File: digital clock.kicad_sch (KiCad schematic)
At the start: 149 parts, among them Q1 BC557, Q10 BC547, Q11 BC547, Q12 BC557, Q13 BC557, Q14 BC557, Q2 BC557, Q3 BC557, Q7 BC557, Q8 BC547, Q9 BC547

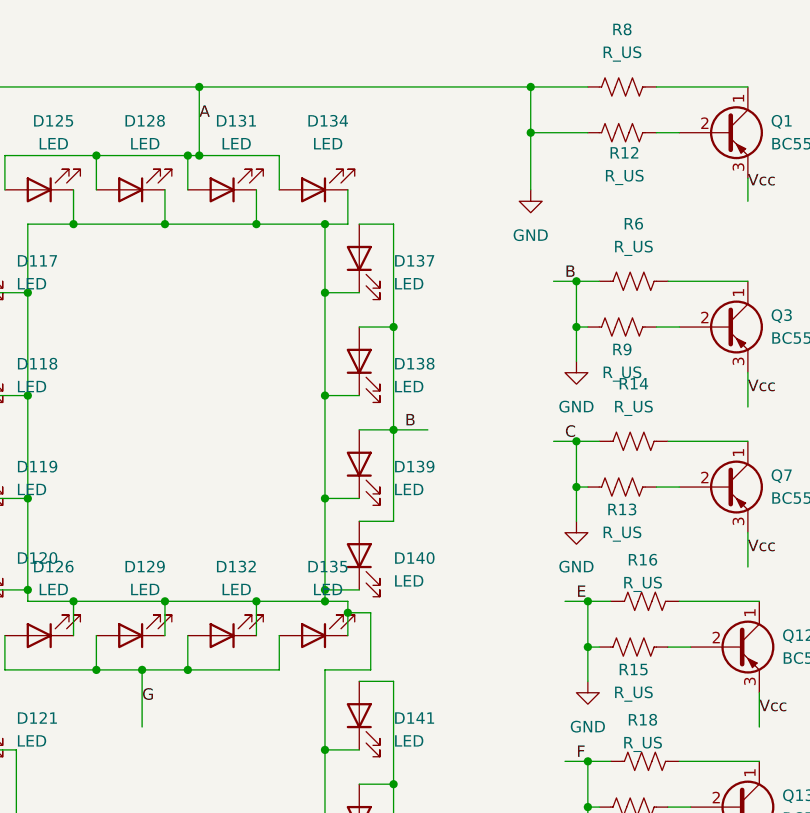
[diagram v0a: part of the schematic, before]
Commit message: correcting transistors
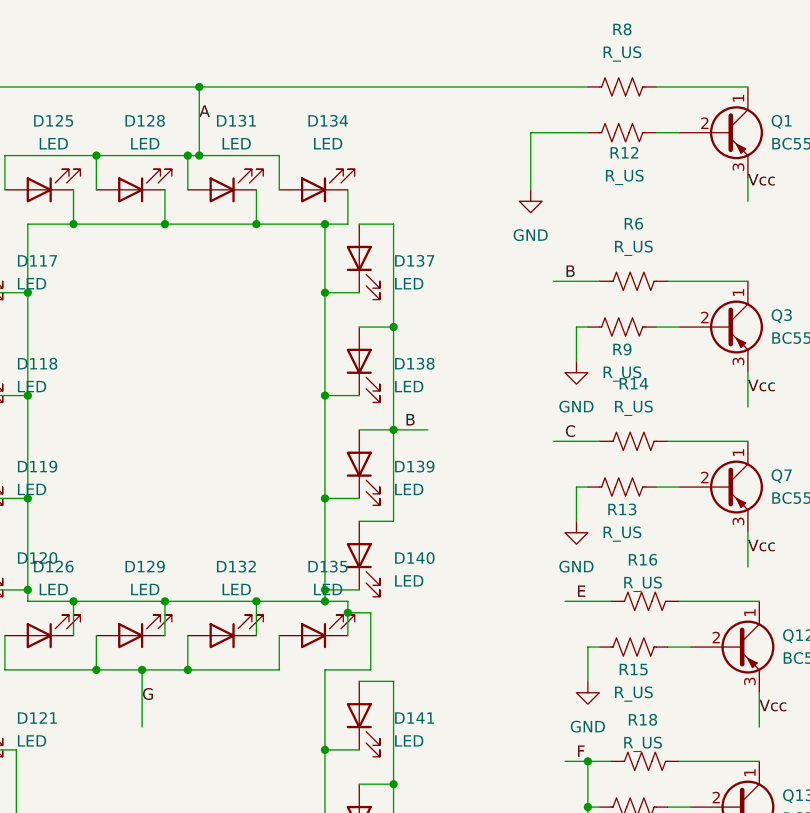
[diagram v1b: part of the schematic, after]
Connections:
- net GND: no longer D102.2 (A), D105.2 (A), D106.2 (A), D107.2 (A), D108.2 (A), D109.2 (A), D110.2 (A), D111.2 (A), D112.2 (A), D121.2 (A), D122.2 (A), D123.2 (A), D124.2 (A), D125.2 (A), D128.2 (A), D131.2 (A), D134.2 (A), D137.2 (A), D138.2 (A), D139.2 (A), D140.2 (A), D141.2 (A), D142.2 (A), D143.2 (A), D144.2 (A), D37.2 (A), D38.2 (A), D39.2 (A), D40.2 (A), D41.2 (A), D44.2 (A), D47.2 (A), D50.2 (A), D53.2 (A), D54.2 (A), D55.2 (A), D56.2 (A), D57.2 (A), D58.2 (A), D59.2 (A), D60.2 (A), D61.2 (A), D62.2 (A), D63.2 (A), D64.2 (A), D65.2 (A), D68.2 (A), D71.2 (A), D74.2 (A), D77.2 (A), D78.2 (A), D79.2 (A), D80.2 (A), D81.2 (A), D82.2 (A), D83.2 (A), D84.2 (A), D89.2 (A), D90.2 (A), D91.2 (A), D92.2 (A), D93.2 (A), D96.2 (A), D99.2 (A), R14.1, R16.1, R6.1, R8.1
- new net A: D102.2 (A), D125.2 (A), D128.2 (A), D131.2 (A), D134.2 (A), D41.2 (A), D44.2 (A), D47.2 (A), D50.2 (A), D65.2 (A), D68.2 (A), D71.2 (A), D74.2 (A), D93.2 (A), D96.2 (A), D99.2 (A), R8.1
- new net B: D105.2 (A), D106.2 (A), D107.2 (A), D108.2 (A), D137.2 (A), D138.2 (A), D139.2 (A), D140.2 (A), D54.2 (A), D56.2 (A), D58.2 (A), D60.2 (A), D77.2 (A), D78.2 (A), D79.2 (A), D80.2 (A), R6.1
- new net C: D109.2 (A), D110.2 (A), D111.2 (A), D112.2 (A), D141.2 (A), D142.2 (A), D143.2 (A), D144.2 (A), D61.2 (A), D62.2 (A), D63.2 (A), D64.2 (A), D81.2 (A), D82.2 (A), D83.2 (A), D84.2 (A), R14.1
- new net E: D121.2 (A), D122.2 (A), D123.2 (A), D124.2 (A), D37.2 (A), D38.2 (A), D39.2 (A), D40.2 (A), D53.2 (A), D55.2 (A), D57.2 (A), D59.2 (A), D89.2 (A), D90.2 (A), D91.2 (A), D92.2 (A), R16.1
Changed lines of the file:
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@@
 	(paper "A2")
 	(junction
-		(at 436.88 81.28)
-		(diameter 0)
-		(color 0 0 0 0)
-	)
-	(junction
 		(at 115.57 107.95)
 		(diameter 0)
@@
 	)
 	(junction
-		(at 443.23 138.43)
-		(diameter 0)
-		(color 0 0 0 0)
-	)
-	(junction
 		(at 157.48 137.16)
 		(diameter 0)
@@
 	)
 	(junction
-		(at 436.88 86.36)
-		(diameter 0)
-		(color 0 0 0 0)
-	)
-	(junction
 		(at 414.02 115.57)
 		(diameter 0)
@@
 	)
 	(junction
-		(at 441.96 102.87)
-		(diameter 0)
-		(color 0 0 0 0)
-	)
-	(junction
 		(at 323.85 88.9)
 		(diameter 0)
@@
 	)
 	(junction
-		(at 443.23 143.51)
-		(diameter 0)
-		(color 0 0 0 0)
-	)
-	(junction
 		(at 219.71 199.39)
 		(diameter 0)
@@
 	)
 	(junction
-		(at 441.96 120.65)
-		(diameter 0)
-		(color 0 0 0 0)
-	)
-	(junction
 		(at 115.57 119.38)
 		(diameter 0)
@@
 	)
 	(junction
-		(at 441.96 107.95)
-		(diameter 0)
-		(color 0 0 0 0)
-	)
-	(junction
 		(at 396.24 189.23)
 		(diameter 0)
@@
 	)
 	(junction
-		(at 441.96 125.73)
-		(diameter 0)
-		(color 0 0 0 0)
-	)
-	(junction
 		(at 237.49 96.52)
 		(diameter 0)
@@
 	(wire
 		(pts
-			(xy 441.96 120.65) (xy 441.96 125.73)
-		)
-		(stroke
-			(width 0)
-			(type default)
-		)
-	)
-	(wire
-		(pts
 			(xy 312.42 189.23) (xy 322.58 189.23)
 		)
@@
 	(wire
 		(pts
-			(xy 436.88 81.28) (xy 443.23 81.28)
-		)
-		(stroke
-			(width 0)
-			(type default)
-		)
-	)
-	(wire
-		(pts
 			(xy 162.56 139.7) (xy 160.02 139.7)
 		)
@@
 	(wire
 		(pts
-			(xy 440.69 138.43) (xy 443.23 138.43)
+			(xy 440.69 138.43) (xy 445.77 138.43)
 		)
 		(stroke
@@
 	(wire
 		(pts
-			(xy 400.05 81.28) (xy 436.88 81.28)
+			(xy 400.05 81.28) (xy 443.23 81.28)
 		)
 		(stroke
@@
 	(wire
 		(pts
-			(xy 441.96 102.87) (xy 441.96 107.95)
-		)
-		(stroke
-			(width 0)
-			(type default)
-		)
-	)
-	(wire
-		(pts
 			(xy 237.49 166.37) (xy 241.3 166.37)
 		)
@@
 	(wire
 		(pts
-			(xy 444.5 120.65) (xy 441.96 120.65)
-		)
-		(stroke
-			(width 0)
-			(type default)
-		)
-	)
-	(wire
-		(pts
 			(xy 199.39 127) (xy 204.47 127)
 		)
@@
 	(wire
 		(pts
-			(xy 444.5 102.87) (xy 441.96 102.87)
-		)
-		(stroke
-			(width 0)
-			(type default)
-		)
-	)
-	(wire
-		(pts
 			(xy 443.23 179.07) (xy 444.5 179.07)
 		)
@@
 	(wire
 		(pts
-			(xy 436.88 81.28) (xy 436.88 86.36)
-		)
-		(stroke
-			(width 0)
-			(type default)
-		)
-	)
-	(wire
-		(pts
 			(xy 312.42 189.23) (xy 312.42 191.77)
 		)
@@
 	(wire
 		(pts
-			(xy 443.23 138.43) (xy 443.23 143.51)
-		)
-		(stroke
-			(width 0)
-			(type default)
-		)
-	)
-	(wire
-		(pts
 			(xy 322.58 189.23) (xy 322.58 191.77)
 		)
@@
 	(wire
 		(pts
-			(xy 439.42 102.87) (xy 441.96 102.87)
+			(xy 439.42 102.87) (xy 444.5 102.87)
 		)
 		(stroke
@@
 	(wire
 		(pts
-			(xy 445.77 138.43) (xy 443.23 138.43)
-		)
-		(stroke
-			(width 0)
-			(type default)
-		)
-	)
-	(wire
-		(pts
 			(xy 157.48 177.8) (xy 157.48 187.96)
 		)
@@
 	(wire
 		(pts
-			(xy 439.42 120.65) (xy 441.96 120.65)
+			(xy 439.42 120.65) (xy 444.5 120.65)
 		)
 		(stroke
@@
 		(on_board yes)
 		(dnp no)
-		(fields_autoplaced yes)
 		(property "Reference" "Q1"
 			(at 463.55 85.0899 0)

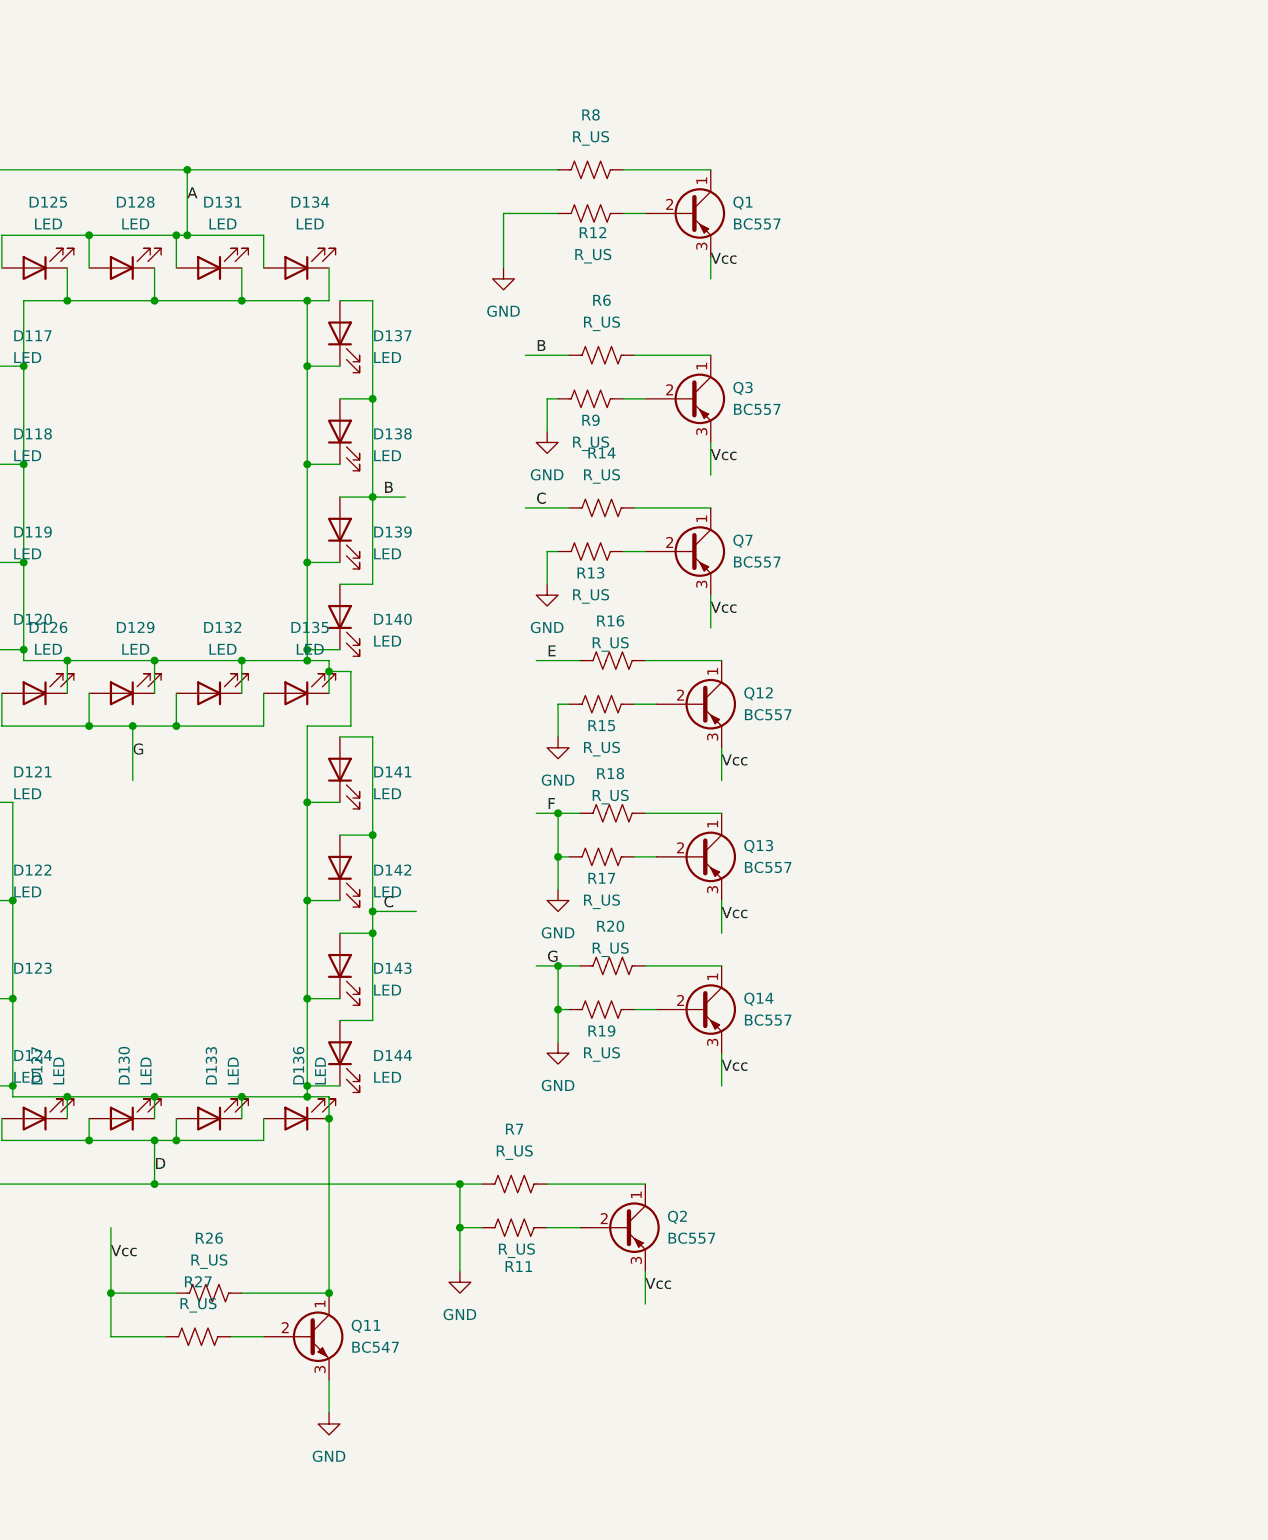
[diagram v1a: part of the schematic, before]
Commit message: transistor correction and LEDs arrangement
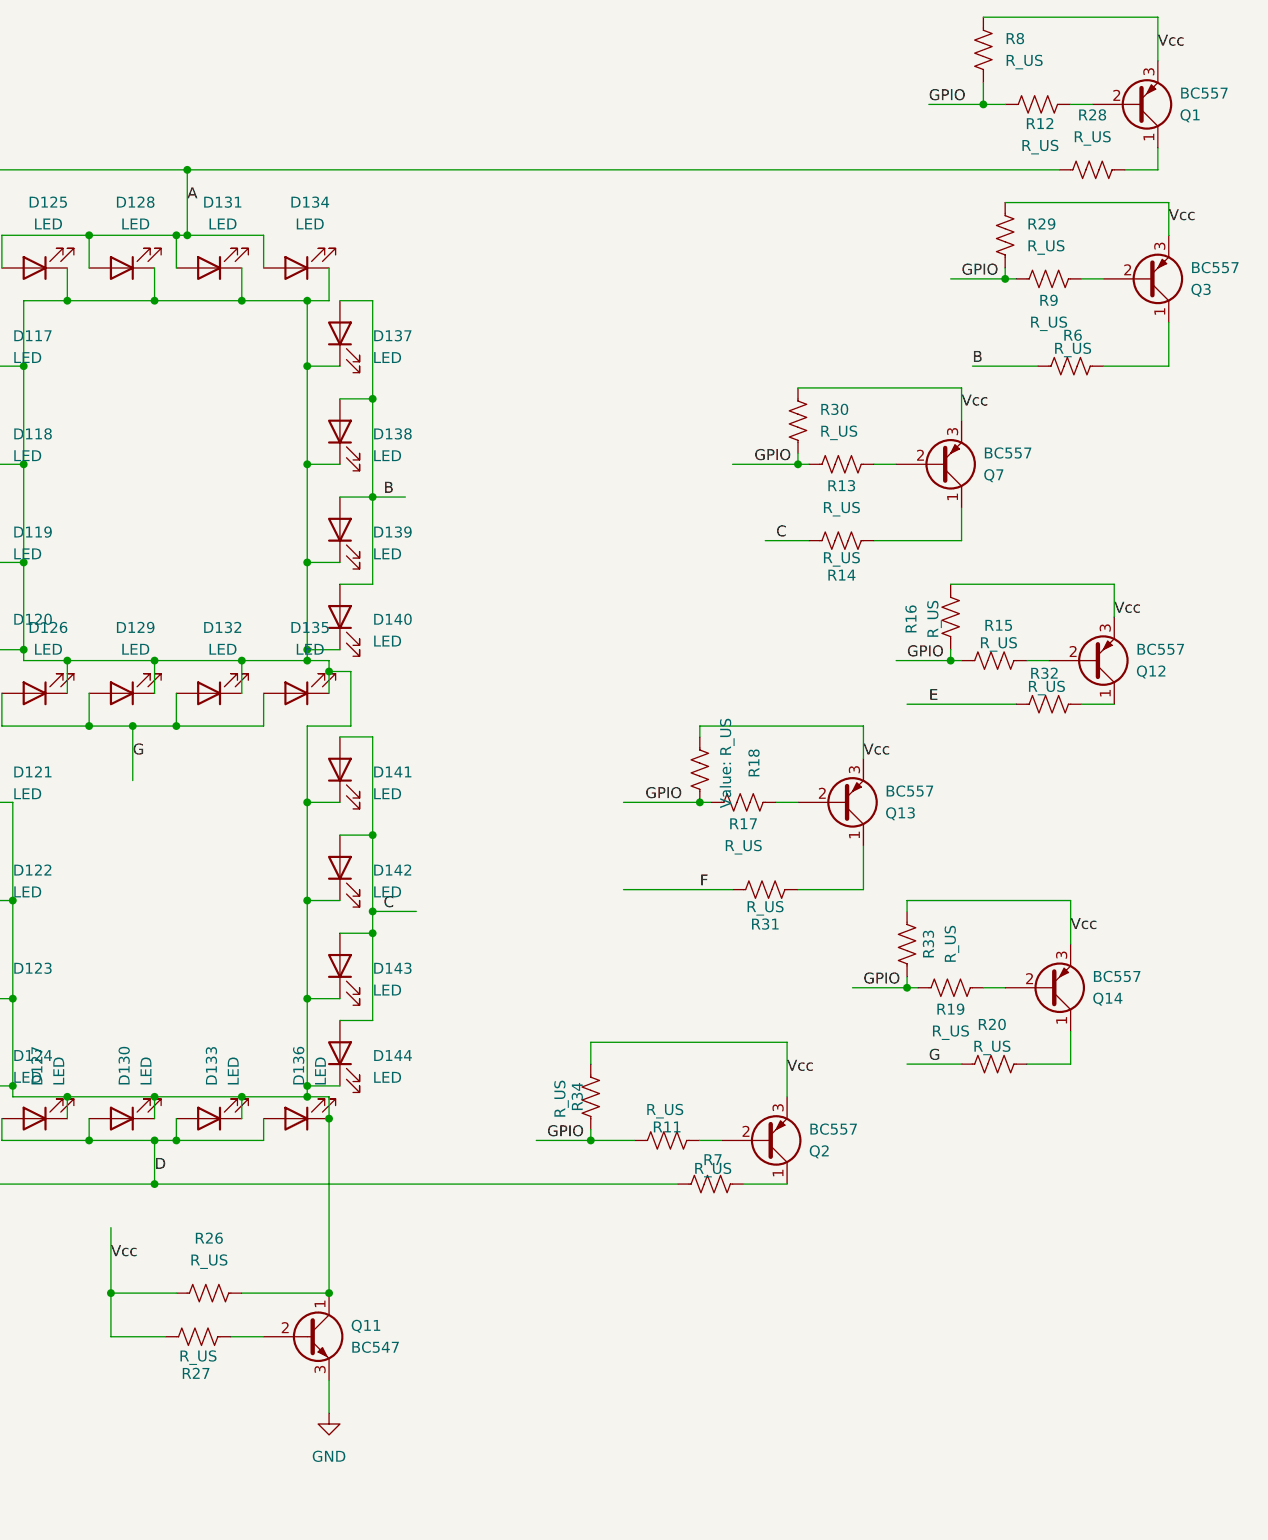
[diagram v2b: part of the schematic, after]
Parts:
- added R28, R29, R30, R31, R32, R33, R34: R_US, Resistor_THT:R_Axial_DIN0207_L6.3mm_D2.5mm_P10.16mm_Horizontal, symbol Device:R_US
- R10, R11, R12, R13, R14, R15, R16, R17, R18, R19, R20, R21, R22, R23, R24, R25, R26, R27, R6, R7, R8, R9: footprint Resistor_THT:R_Axial_DIN0204_L3.6mm_D1.6mm_P7.62mm_Horizontal -> Resistor_THT:R_Axial_DIN0207_L6.3mm_D2.5mm_P10.16mm_Horizontal
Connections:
- net A: now also R28.1; no longer R8.1
- net E: now also R32.1; no longer R16.1
- net GND: no longer D100.2 (A), D101.2 (A), D103.2 (A), D104.2 (A), D117.2 (A), D118.2 (A), D119.2 (A), D120.2 (A), D126.2 (A), D127.2 (A), D129.2 (A), D130.2 (A), D132.2 (A), D133.2 (A), D135.2 (A), D136.2 (A), D23.2 (A), D25.2 (A), D27.2 (A), D32.2 (A), D33.2 (A), D34.2 (A), D35.2 (A), D36.2 (A), D42.2 (A), D43.2 (A), D45.2 (A), D46.2 (A), D48.2 (A), D49.2 (A), D51.2 (A), D52.2 (A), D66.2 (A), D67.2 (A), D69.2 (A), D70.2 (A), D72.2 (A), D73.2 (A), D75.2 (A), D76.2 (A), D85.2 (A), D86.2 (A), D87.2 (A), D88.2 (A), D94.2 (A), D95.2 (A), D97.2 (A), D98.2 (A), R11.1, R12.2, R13.1, R15.1, R17.1, R18.1, R19.1, R20.1, R7.1, R9.1
- net Vcc: now also R16.2, R18.2, R8.2, R29.1, R30.1, R33.2, R34.2
- net at Q1.1 (C): now also R28.2; no longer R8.2
- net at Q13.1 (C): now also R31.2; no longer R18.2
- net at Q12.1 (C): now also R32.2; no longer R16.2
- new net D: D101.2 (A), D104.2 (A), D127.2 (A), D130.2 (A), D133.2 (A), D136.2 (A), D43.2 (A), D46.2 (A), D49.2 (A), D52.2 (A), D67.2 (A), D70.2 (A), D73.2 (A), D76.2 (A), D95.2 (A), D98.2 (A), R7.1
- new net F: D117.2 (A), D118.2 (A), D119.2 (A), D120.2 (A), D23.2 (A), D25.2 (A), D27.2 (A), D32.2 (A), D33.2 (A), D34.2 (A), D35.2 (A), D36.2 (A), D85.2 (A), D86.2 (A), D87.2 (A), D88.2 (A), R31.1
- new net G: D100.2 (A), D103.2 (A), D126.2 (A), D129.2 (A), D132.2 (A), D135.2 (A), D42.2 (A), D45.2 (A), D48.2 (A), D51.2 (A), D66.2 (A), D69.2 (A), D72.2 (A), D75.2 (A), D94.2 (A), D97.2 (A), R20.1
- new net GPIO: R11.1, R12.2, R13.1, R15.1, R16.1, R17.1, R18.1, R19.1, R29.2, R30.2, R33.1, R34.1, R8.1, R9.1
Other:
- moved on the sheet: Q12, Q13, Q14, Q2, Q3, Q7, R11, R13, R15, R16, R17, R18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

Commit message: Changes to be committed:
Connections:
- removed net GPIO: R11.1, R12.2, R13.1, R15.1, R16.1, R17.1, R18.1, R19.1, R29.2, R30.2, R33.1, R34.1, R8.1, R9.1
- new net Led A: R12.2, R8.1
- new net Led B: R29.2, R9.1
- new net Led C: R13.1, R30.2
- new net Led D: R11.1, R34.1
- new net Led E: R15.1, R16.1
- new net Led F: R17.1, R18.1
- new net Led G: R19.1, R33.1
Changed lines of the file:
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@@
 		)
 	)
-	(label "GPIO"
+	(label "Led F"
 		(at 453.39 154.94 0)
 		(fields_autoplaced yes)
@@
 		)
 	)
-	(label "GPIO"
+	(label "Led C"
 		(at 466.09 115.57 0)
 		(fields_autoplaced yes)
@@
 		)
 	)
-	(label "GPIO"
+	(label "Led G"
 		(at 478.79 176.53 0)
 		(fields_autoplaced yes)
@@
 		)
 	)
-	(label "GPIO"
+	(label "Led D"
 		(at 441.96 194.31 0)
 		(fields_autoplaced yes)
@@
 		)
 	)
-	(label "GPIO"
+	(label "Led A"
 		(at 486.41 73.66 0)
 		(fields_autoplaced yes)
@@
 		)
 	)
-	(label "GPIO"
+	(label "Led E"
 		(at 483.87 138.43 0)
 		(fields_autoplaced yes)
@@
 		)
 	)
-	(label "GPIO"
+	(label "Led B"
 		(at 490.22 93.98 0)
 		(fields_autoplaced yes)

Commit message: value addition & led arrangement
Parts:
- R10, R16, R18, R21, R24, R26, R29, R30, R33, R34, R8: value R_US -> 1k
- R11, R12, R13, R15, R17, R19, R22, R23, R25, R27, R9: value R_US -> 10k
- R14, R20, R28, R31, R32, R6, R7: value R_US -> 33
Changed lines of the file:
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@@
 			)
 		)
-		(property "Value" "R_US"
+		(property "Value" "10k"
 			(at 494.538 136.398 90)
 			(effects
@@
 		(on_board yes)
 		(dnp no)
-		(fields_autoplaced yes)
 		(property "Reference" "Q9"
 			(at 242.57 214.6299 0)
@@
 		(dnp no)
 		(property "Reference" "R9"
-			(at 500.38 96.52 90)
+			(at 500.38 95.25 90)
 			(effects
 				(font
@@
 			)
 		)
-		(property "Value" "R_US"
-			(at 500.38 99.06 90)
+		(property "Value" "10k"
+			(at 500.634 96.774 90)
 			(effects
 				(font
@@
 			)
 		)
-		(property "Value" "R_US"
+		(property "Value" "33"
 			(at 493.776 183.388 90)
 			(effects
@@
 			)
 		)
-		(property "Value" "R_US"
+		(property "Value" "33"
 			(at 461.264 197.612 90)
 			(effects
@@
 			)
 		)
-		(property "Value" "R_US"
+		(property "Value" "10k"
 			(at 464.82 160.02 90)
 			(effects
@@
 			)
 		)
-		(property "Value" "R_US"
+		(property "Value" "10k"
 			(at 476.25 120.65 90)
 			(effects
@@
 		(on_board yes)
 		(dnp no)
-		(fields_autoplaced yes)
 		(property "Reference" "R25"
-			(at 328.93 209.55 90)
+			(at 329.184 218.186 90)
 			(effects
 				(font
@@
 			)
 		)
-		(property "Value" "R_US"
-			(at 328.93 212.09 90)
+		(property "Value" "10k"
+			(at 328.93 214.376 90)
 			(effects
 				(font
@@
 			)
 		)
-		(property "Value" "R_US"
+		(property "Value" "10k"
 			(at 223.52 220.472 90)
 			(effects
@@
 		(on_board yes)
 		(dnp no)
-		(fields_autoplaced yes)
 		(property "Reference" "R22"
-			(at 143.51 210.82 90)
+			(at 143.002 213.106 90)
 			(effects
 				(font
@@
 			)
 		)
-		(property "Value" "R_US"
-			(at 143.51 213.36 90)
+		(property "Value" "10k"
+			(at 143.256 214.63 90)
 			(effects
 				(font
@@
 			)
 		)
-		(property "Value" "R_US"
+		(property "Value" "1k"
 			(at 443.484 189.484 90)
 			(effects
@@
 			)
 		)
-		(property "Value" "R_US"
+		(property "Value" "10k"
 			(at 455.676 190.754 90)
 			(effects
@@
 		(on_board yes)
 		(dnp no)
-		(fields_autoplaced yes)
 		(property "Reference" "R21"
-			(at 223.52 204.47 90)
+			(at 223.52 207.01 90)
 			(effects
 				(font
@@
 			)
 		)
-		(property "Value" "R_US"
-			(at 223.52 207.01 90)
+		(property "Value" "1k"
+			(at 223.52 208.788 90)
 			(effects
 				(font
@@
 			)
 		)
-		(property "Value" "R_US"
+		(property "Value" "33"
 			(at 467.36 167.132 90)
 			(effects
@@
 			)
 		)
-		(property "Value" "R_US"
+		(property "Value" "1k"
 			(at 488.95 171.45 90)
 			(effects
@@
 		(on_board yes)
 		(dnp no)
-		(fields_autoplaced yes)
 		(property "Reference" "R28"
-			(at 505.46 74.93 90)
+			(at 506.222 78.232 90)
 			(effects
 				(font
@@
 			)
 		)
-		(property "Value" "R_US"
-			(at 505.46 77.47 90)
+		(property "Value" "33"
+			(at 505.714 80.01 90)
 			(effects
 				(font
@@
 			)
 		)
-		(property "Value" "R_US"
+		(property "Value" "1k"
 			(at 473.71 111.7599 0)
 			(effects
@@
 			)
 		)
-		(property "Value" "R_US"
+		(property "Value" "10k"
 			(at 499.364 78.486 90)
 			(effects
@@
 		(on_board yes)
 		(dnp no)
-		(fields_autoplaced yes)
 		(property "Reference" "R24"
-			(at 332.74 204.47 90)
+			(at 332.994 206.756 90)
 			(effects
 				(font
@@
 			)
 		)
-		(property "Value" "R_US"
-			(at 332.74 207.01 90)
+		(property "Value" "1k"
+			(at 332.74 208.28 90)
 			(effects
 				(font
@@
 			)
 		)
-		(property "Value" "R_US"
+		(property "Value" "10k"
 			(at 488.95 181.61 90)
 			(effects
@@
 			)
 		)
-		(property "Value" "R_US"
+		(property "Value" "1k"
 			(at 495.3 68.5799 0)
 			(effects
@@
 		(dnp no)
 		(property "Reference" "R18"
-			(at 466.09 150.368 90)
+			(at 462.28 150.622 90)
 			(effects
 				(font
@@
 			)
 		)
-		(property "Value" "R_US"
-			(at 462.788 150.368 90)
-			(show_name yes)
+		(property "Value" "1k"
+			(at 457.708 150.622 90)
 			(effects
 				(font
@@
 			)
 		)
-		(property "Value" "R_US"
+		(property "Value" "33"
 			(at 503.174 102.108 90)
 			(effects
@@
 			)
 		)
-		(property "Value" "R_US"
+		(property "Value" "33"
 			(at 500.126 141.478 90)
 			(effects
@@
 			)
 		)
-		(property "Value" "R_US"
+		(property "Value" "1k"
 			(at 148.59 208.28 90)
 			(effects
@@
 			)
 		)
-		(property "Value" "R_US"
+		(property "Value" "33"
 			(at 476.25 126.492 90)
 			(effects
@@
 			)
 		)
-		(property "Value" "R_US"
+		(property "Value" "10k"
 			(at 401.32 219.456 90)
 			(effects
@@
 			)
 		)
-		(property "Value" "R_US"
+		(property "Value" "1k"
 			(at 402.59 208.28 90)
 			(effects
@@
 			)
 		)
-		(property "Value" "R_US"
+		(property "Value" "1k"
 			(at 497.84 90.1699 0)
 			(effects
@@
 			)
 		)
-		(property "Value" "R_US"
+		(property "Value" "1k"
 			(at 486.918 133.604 90)
 			(effects
